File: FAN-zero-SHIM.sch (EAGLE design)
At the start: 4 parts

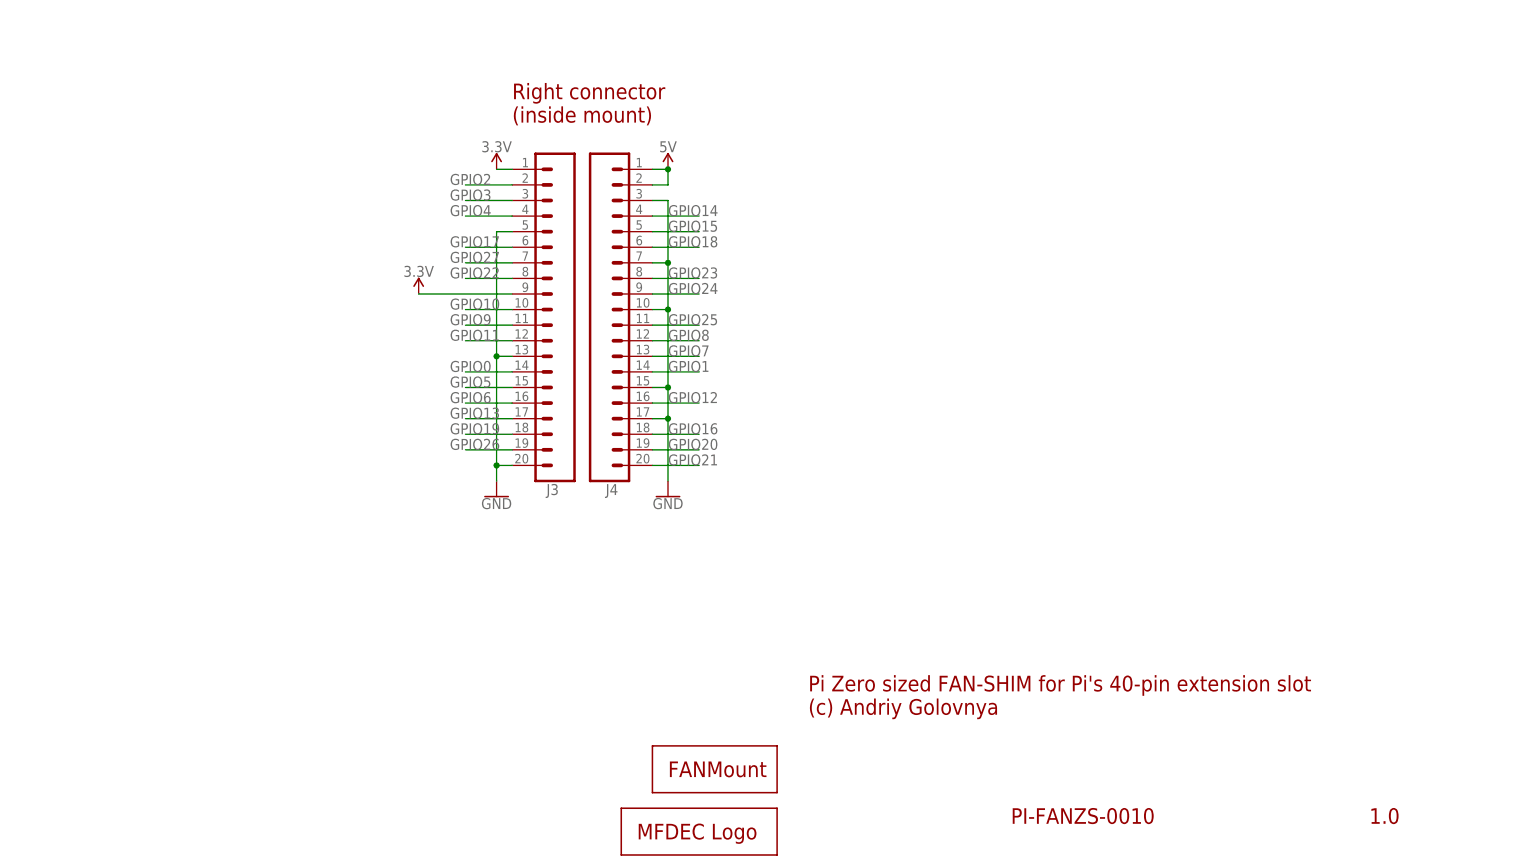
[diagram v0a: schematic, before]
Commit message: Added basic placement for zero board
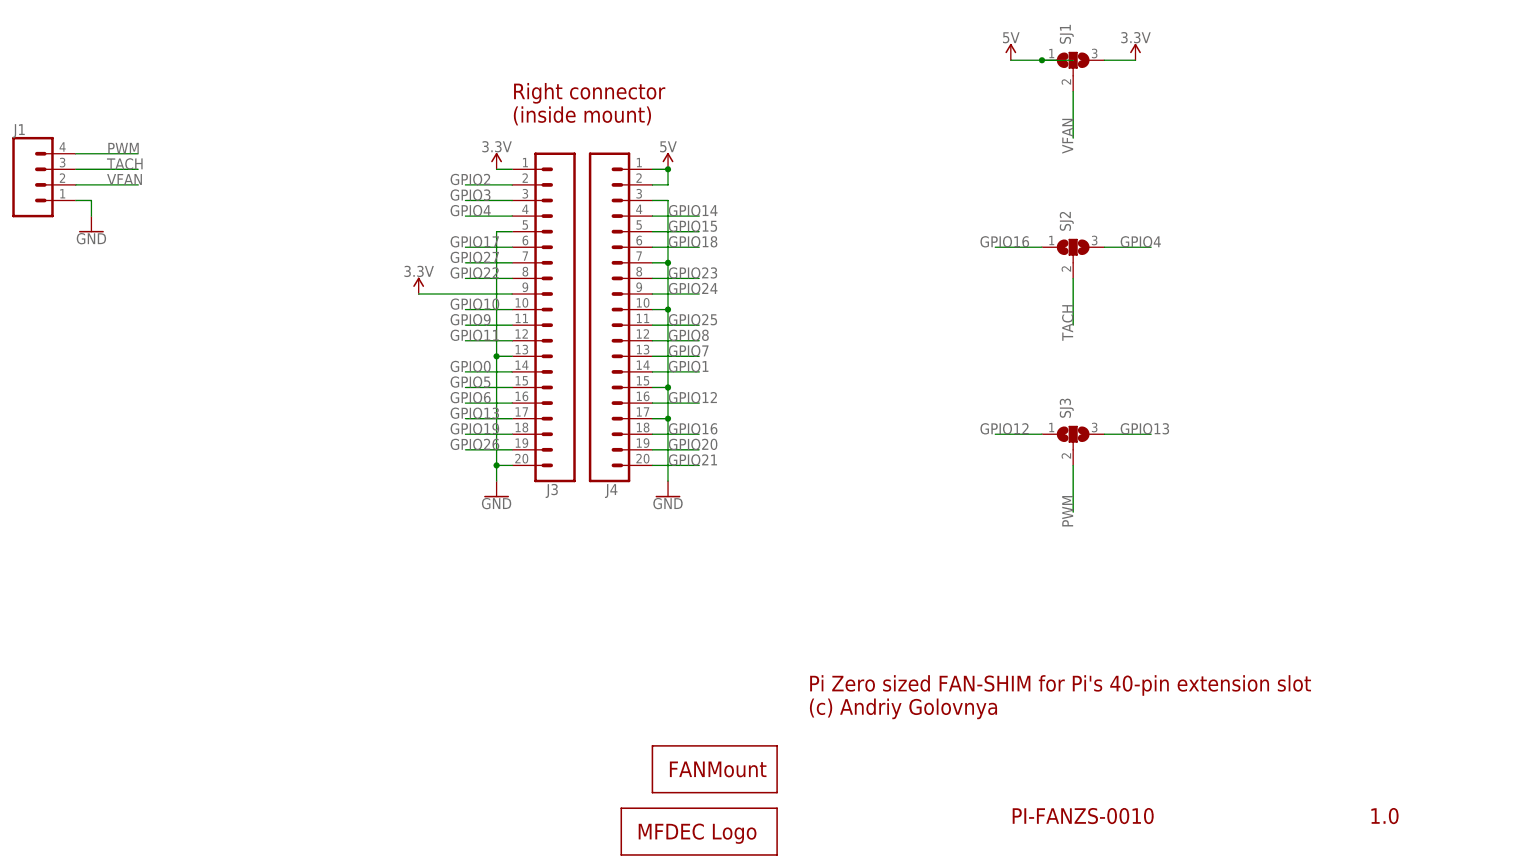
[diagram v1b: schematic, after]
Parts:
- added J1: (no value), SparkFun-Connectors:CONN_04
- added SJ1, SJ2, SJ3: (no value), _my_jumpers:SJ2
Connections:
- new net PWM: J1.4, SJ3.2
- new net TACH: J1.3, SJ2.2
- new net VFAN: J1.2, SJ1.2
- net 3.3V: now also SJ1.3
- net 5V: now also SJ1.1
- net GND: now also J1.1
- net GPIO12: now also SJ3.1
- net GPIO13: now also SJ3.3
- net GPIO16: now also SJ2.1
- net GPIO4: now also SJ2.3
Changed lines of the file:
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@@
 <part name="LOGO1" library="_my_logos" deviceset="MFDECLOGO" device="_L_30MM"/>
 <part name="FAN1" library="_my_fans" deviceset="FAN" device="30HO"/>
+<part name="J1" library="SparkFun-Connectors" library_urn="urn:adsk.eagle:library:513" deviceset="CONN_04" device="" package3d_urn="urn:adsk.eagle:package:38085/1"/>
+<part name="GND1" library="SparkFun-PowerSymbols" library_urn="urn:adsk.eagle:library:530" deviceset="GND" device=""/>
+<part name="SJ1" library="_my_jumpers" deviceset="SJ2" device=""/>
+<part name="SJ2" library="_my_jumpers" deviceset="SJ2" device=""/>
+<part name="SJ3" library="_my_jumpers" deviceset="SJ2" device=""/>
+<part name="SUPPLY1" library="SparkFun-PowerSymbols" library_urn="urn:adsk.eagle:library:530" deviceset="5V" device=""/>
+<part name="SUPPLY3" library="SparkFun-PowerSymbols" library_urn="urn:adsk.eagle:library:530" deviceset="3.3V" device=""/>
 </parts>
 <sheets>
@@
 <instance part="LOGO1" gate="G$1" x="134.62" y="2.54" smashed="yes"/>
 <instance part="FAN1" gate="G$1" x="139.7" y="12.7" smashed="yes"/>
+<instance part="J1" gate="G$1" x="40.64" y="111.76" smashed="yes">
+<attribute name="VALUE" x="35.56" y="104.394" size="1.778" layer="96" font="vector"/>
+<attribute name="NAME" x="35.56" y="119.888" size="1.778" layer="95" font="vector"/>
+</instance>
+<instance part="GND1" gate="1" x="48.26" y="104.14" smashed="yes">
+<attribute name="VALUE" x="48.26" y="103.886" size="1.778" layer="96" align="top-center"/>
+</instance>
+<instance part="SJ1" gate="G$1" x="208.28" y="132.08" smashed="yes" rot="R90">
+<attribute name="NAME" x="207.899" y="134.62" size="1.778" layer="95" rot="R90"/>
+<attribute name="VALUE" x="210.185" y="134.62" size="1.778" layer="96" rot="R90"/>
+</instance>
+<instance part="SJ2" gate="G$1" x="208.28" y="101.6" smashed="yes" rot="R90">
+<attribute name="NAME" x="207.899" y="104.14" size="1.778" layer="95" rot="R90"/>
+<attribute name="VALUE" x="210.185" y="104.14" size="1.778" layer="96" rot="R90"/>
+</instance>
+<instance part="SJ3" gate="G$1" x="208.28" y="71.12" smashed="yes" rot="R90">
+<attribute name="NAME" x="207.899" y="73.66" size="1.778" layer="95" rot="R90"/>
+<attribute name="VALUE" x="210.185" y="73.66" size="1.778" layer="96" rot="R90"/>
+</instance>
+<instance part="SUPPLY1" gate="G$1" x="198.12" y="132.08" smashed="yes">
+<attribute name="VALUE" x="198.12" y="134.874" size="1.778" layer="96" align="bottom-center"/>
+</instance>
+<instance part="SUPPLY3" gate="G$1" x="218.44" y="132.08" smashed="yes">
+<attribute name="VALUE" x="218.44" y="134.874" size="1.778" layer="96" align="bottom-center"/>
+</instance>
 </instances>
 <busses>
@@
 <wire x1="116.84" y1="93.98" x2="101.6" y2="93.98" width="0.1524" layer="91"/>
 <pinref part="SUPPLY9" gate="G$1" pin="3.3V"/>
+</segment>
+<segment>
+<wire x1="213.36" y1="132.08" x2="218.44" y2="132.08" width="0.1524" layer="91"/>
+<pinref part="SJ1" gate="G$1" pin="3"/>
+<pinref part="SUPPLY3" gate="G$1" pin="3.3V"/>
 </segment>
 </net>
@@
 <junction x="142.24" y="73.66"/>
 </segment>
+<segment>
+<wire x1="45.72" y1="109.22" x2="48.26" y2="109.22" width="0.1524" layer="91"/>
+<wire x1="48.26" y1="109.22" x2="48.26" y2="106.68" width="0.1524" layer="91"/>
+<pinref part="J1" gate="G$1" pin="1"/>
+<pinref part="GND1" gate="1" pin="GND"/>
+</segment>
 </net>
 <net name="GPIO2" class="0">
@@
 <label x="106.68" y="106.68" size="1.778" layer="95"/>
 </segment>
+<segment>
+<wire x1="213.36" y1="101.6" x2="220.98" y2="101.6" width="0.1524" layer="91"/>
+<label x="215.9" y="101.6" size="1.778" layer="95"/>
+<pinref part="SJ2" gate="G$1" pin="3"/>
+</segment>
 </net>
 <net name="GPIO17" class="0">
@@
 <label x="106.68" y="73.66" size="1.778" layer="95"/>
 </segment>
+<segment>
+<wire x1="213.36" y1="71.12" x2="220.98" y2="71.12" width="0.1524" layer="91"/>
+<label x="215.9" y="71.12" size="1.778" layer="95"/>
+<pinref part="SJ3" gate="G$1" pin="3"/>
+</segment>
 </net>
 <net name="GPIO19" class="0">
@@
 <label x="142.24" y="76.2" size="1.778" layer="95"/>
 </segment>
+<segment>
+<wire x1="203.2" y1="71.12" x2="195.58" y2="71.12" width="0.1524" layer="91"/>
+<label x="193.04" y="71.12" size="1.778" layer="95"/>
+<pinref part="SJ3" gate="G$1" pin="1"/>
+</segment>
 </net>
 <net name="GPIO16" class="0">
@@
 <wire x1="139.7" y1="71.12" x2="147.32" y2="71.12" width="0.1524" layer="91"/>
 <label x="142.24" y="71.12" size="1.778" layer="95"/>
+</segment>
+<segment>
+<wire x1="203.2" y1="101.6" x2="195.58" y2="101.6" width="0.1524" layer="91"/>
+<label x="193.04" y="101.6" size="1.778" layer="95"/>
+<pinref part="SJ2" gate="G$1" pin="1"/>
 </segment>
 </net>
@@
 <pinref part="SUPPLY2" gate="G$1" pin="5V"/>
 <junction x="142.24" y="114.3"/>
+</segment>
+<segment>
+<wire x1="203.2" y1="132.08" x2="198.12" y2="132.08" width="0.1524" layer="91"/>
+<wire x1="203.2" y1="132.08" x2="208.28" y2="132.08" width="0.1524" layer="91"/>
+<junction x="203.2" y="132.08"/>
+<pinref part="SJ1" gate="G$1" pin="1"/>
+<pinref part="SUPPLY1" gate="G$1" pin="5V"/>
+</segment>
+</net>
+<net name="VFAN" class="0">
+<segment>
+<wire x1="45.72" y1="111.76" x2="55.88" y2="111.76" width="0.1524" layer="91"/>
+<label x="50.8" y="111.76" size="1.778" layer="95"/>
+<pinref part="J1" gate="G$1" pin="2"/>
+</segment>
+<segment>
+<wire x1="208.28" y1="127" x2="208.28" y2="119.38" width="0.1524" layer="91"/>
+<label x="208.28" y="116.84" size="1.778" layer="95" rot="R90"/>
+<pinref part="SJ1" gate="G$1" pin="2"/>
+</segment>
+</net>
+<net name="TACH" class="0">
+<segment>
+<wire x1="45.72" y1="114.3" x2="55.88" y2="114.3" width="0.1524" layer="91"/>
+<label x="50.8" y="114.3" size="1.778" layer="95"/>
+<pinref part="J1" gate="G$1" pin="3"/>
+</segment>
+<segment>
+<wire x1="208.28" y1="96.52" x2="208.28" y2="88.9" width="0.1524" layer="91"/>
+<label x="208.28" y="86.36" size="1.778" layer="95" rot="R90"/>
+<pinref part="SJ2" gate="G$1" pin="2"/>
+</segment>
+</net>
+<net name="PWM" class="0">
+<segment>
+<wire x1="45.72" y1="116.84" x2="55.88" y2="116.84" width="0.1524" layer="91"/>
+<label x="50.8" y="116.84" size="1.778" layer="95"/>
+<pinref part="J1" gate="G$1" pin="4"/>
+</segment>
+<segment>
+<wire x1="208.28" y1="66.04" x2="208.28" y2="58.42" width="0.1524" layer="91"/>
+<label x="208.28" y="55.88" size="1.778" layer="95" rot="R90"/>
+<pinref part="SJ3" gate="G$1" pin="2"/>
 </segment>
 </net>
@@
 will not be understood (or retained) with this version.
 </note>
+<note version="8.3" severity="warning">
+Since Version 8.3, EAGLE supports the association of 3D packages
+with devices in libraries, schematics, and board files. Those 3D
+packages will not be understood (or retained) with this version.
+</note>
 </compatibility>
